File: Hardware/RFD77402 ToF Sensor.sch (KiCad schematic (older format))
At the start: 18 parts, among them J1 Qwiic_Connector, J2 Qwiic_Connector, J3 CONN_01X01, J4 I2C_Standard_PTH_Connector, U1 RFD77402, U2 SPARKX-LOGO4, U3 SPARKX-LOGO4, U4 CC_LICENSE

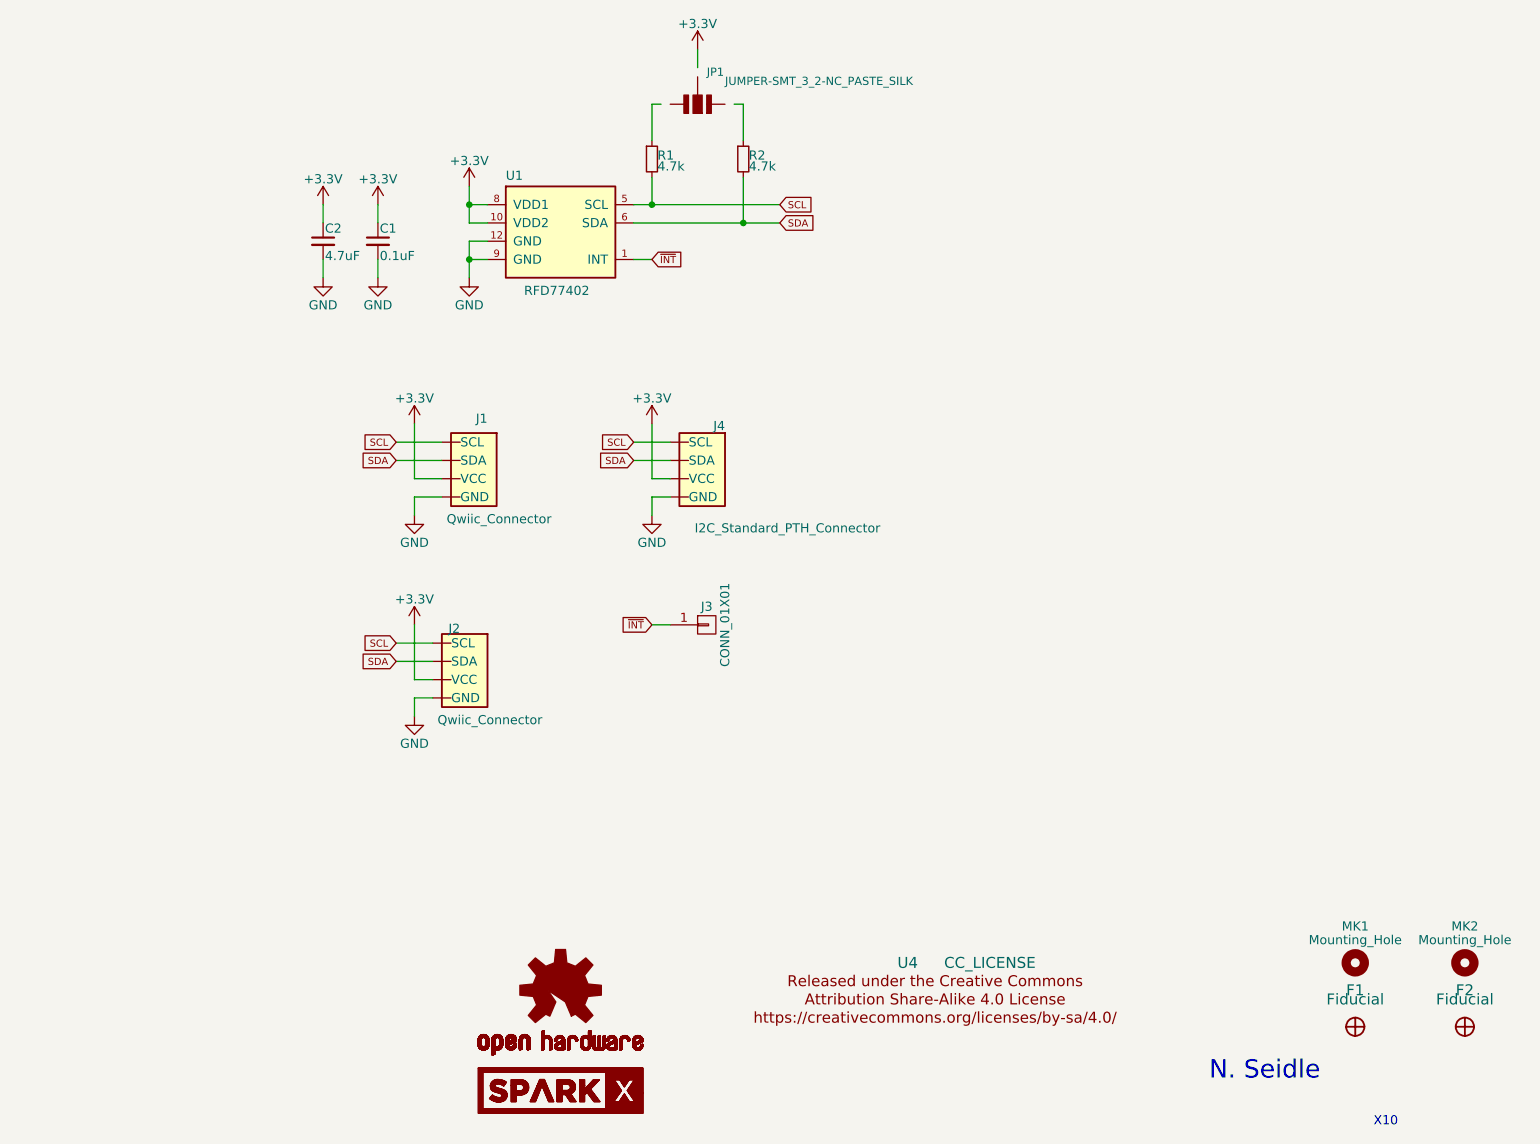
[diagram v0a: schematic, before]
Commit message: Decreasing paste on sensor
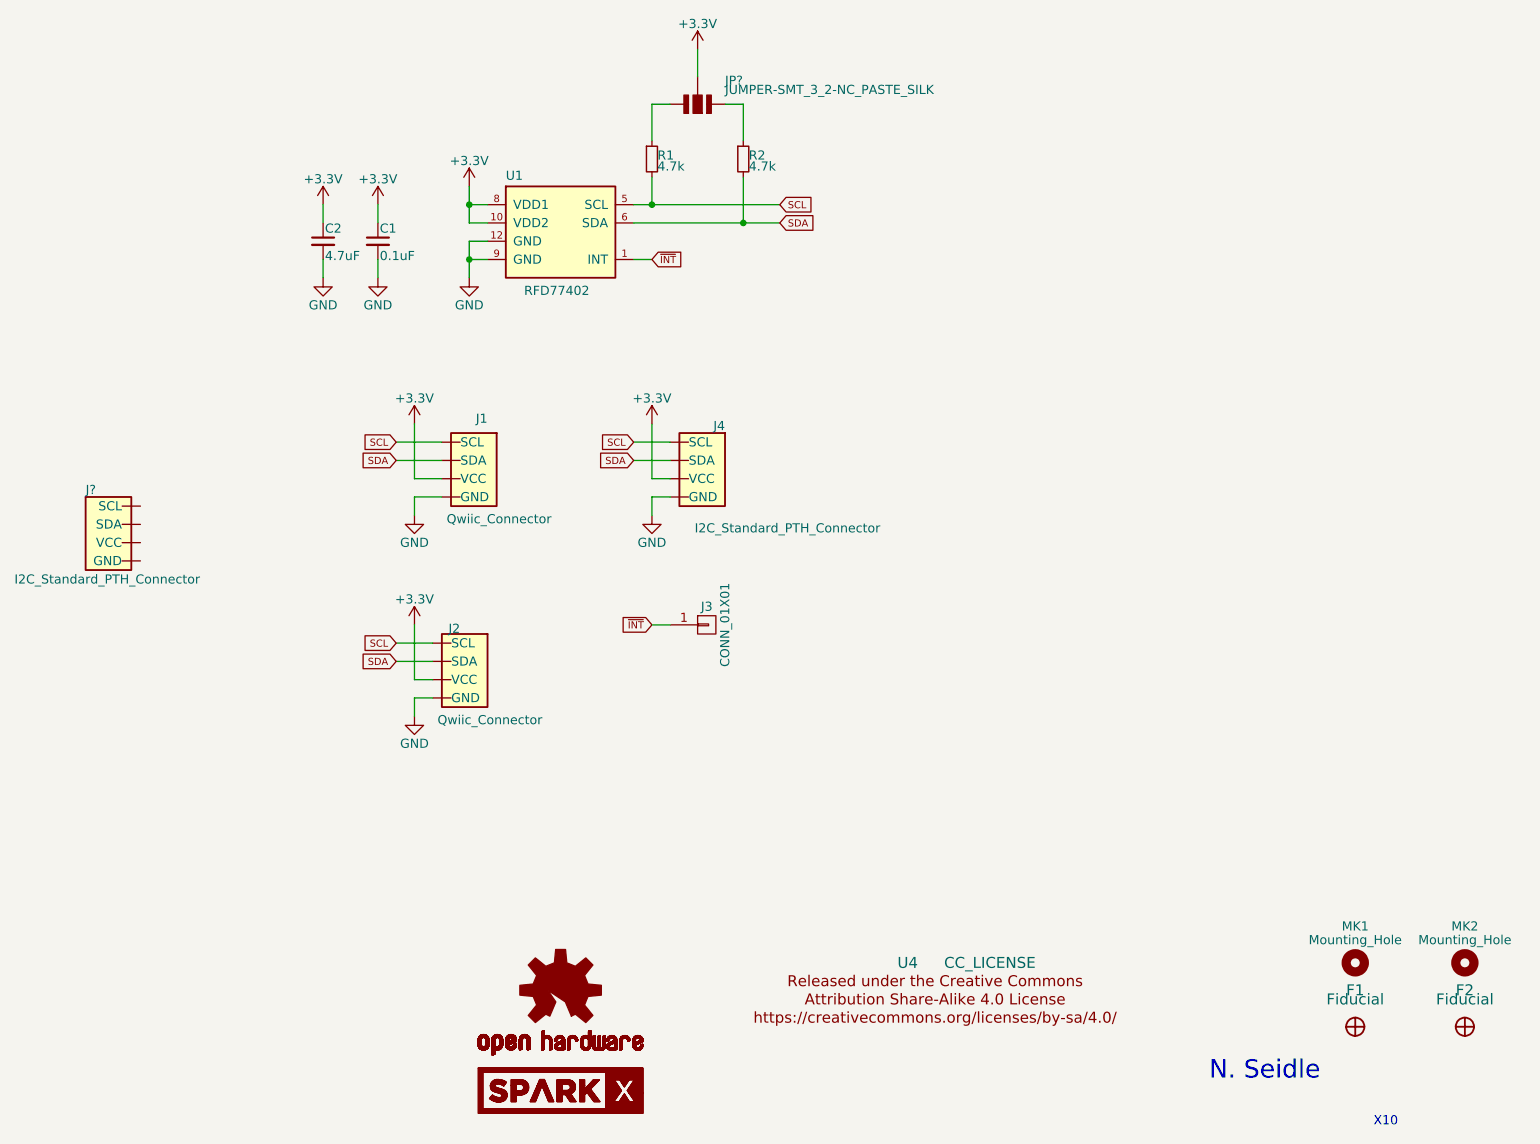
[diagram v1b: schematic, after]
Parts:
- removed JP1: JUMPER-SMT_3_2-NC_PASTE_SILK, SparkFun-Jumpers:SMT-JUMPER_3_2-NC_PASTE_SILK, symbol JUMPER-SMT_3_2-NC_PASTE_SILK
- added J?: I2C_Standard_PTH_Connector, symbol I2C_Standard_PTH_Connector
- added JP?: JUMPER-SMT_3_2-NC_PASTE_SILK, symbol JUMPER-SMT_3_2-NC_PASTE_SILK
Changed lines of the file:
@@
 EESchema Schematic File Version 2
+LIBS:RFD77402 ToF Sensor-rescue
+LIBS:74xgxx
+LIBS:74xx
+LIBS:ac-dc
+LIBS:actel
+LIBS:adc-dac
+LIBS:allegro
+LIBS:Altera
+LIBS:analog_devices
+LIBS:analog_switches
+LIBS:atmel
+LIBS:audio
+LIBS:battery_management
+LIBS:bbd
+LIBS:bosch
+LIBS:brooktre
+LIBS:cmos_ieee
+LIBS:cmos4000
+LIBS:conn
+LIBS:contrib
+LIBS:cypress
+LIBS:dc-dc
+LIBS:device
+LIBS:digital-audio
+LIBS:diode
+LIBS:display
+LIBS:dsp
+LIBS:elec-unifil
+LIBS:ESD_Protection
+LIBS:ftdi
+LIBS:gennum
+LIBS:graphic
+LIBS:hc11
+LIBS:intel
+LIBS:interface
+LIBS:ir
+LIBS:Lattice
+LIBS:leds
+LIBS:linear
+LIBS:logo
+LIBS:maxim
+LIBS:mechanical
+LIBS:memory
+LIBS:microchip
+LIBS:microchip_dspic33dsc
+LIBS:microchip_pic10mcu
+LIBS:microchip_pic12mcu
+LIBS:microchip_pic16mcu
+LIBS:microchip_pic18mcu
+LIBS:microchip_pic24mcu
+LIBS:microchip_pic32mcu
+LIBS:microcontrollers
+LIBS:modules
+LIBS:motor_drivers
+LIBS:motorola
+LIBS:motors
+LIBS:msp430
+LIBS:nordicsemi
+LIBS:nxp
+LIBS:nxp_armmcu
+LIBS:onsemi
+LIBS:opto
+LIBS:Oscillators
+LIBS:philips
 LIBS:power
-LIBS:conn
-LIBS:device
-LIBS:leds
-LIBS:mechanical
-LIBS:SparkFun-LED
-LIBS:SparkFun-Clocks
-LIBS:SparkFun-Aesthetics
-LIBS:SparkFun-Batteries
-LIBS:SparkFun-Boards
-LIBS:SparkFun-Capacitors
-LIBS:SparkFun-Coils
-LIBS:SparkFun-Connectors
-LIBS:SparkFun-DiscreteSemi
-LIBS:SparkFun-Electromechanical
-LIBS:SparkFun-Fuses
-LIBS:SparkFun-GPS
-LIBS:SparkFun-Hardware
-LIBS:SparkFun-IC-Amplifiers
-LIBS:SparkFun-Jumpers
+LIBS:Power_Management
+LIBS:powerint
+LIBS:pspice
+LIBS:references
+LIBS:regul
+LIBS:relays
+LIBS:rfcom
+LIBS:sensors
+LIBS:silabs
+LIBS:siliconi
+LIBS:stm8
+LIBS:stm32
+LIBS:supertex
+LIBS:switches
+LIBS:texas
+LIBS:transf
+LIBS:transistors
+LIBS:triac_thyristor
+LIBS:ttl_ieee
+LIBS:valves
+LIBS:video
+LIBS:wiznet
+LIBS:Worldsemi
+LIBS:Xicor
+LIBS:xilinx
+LIBS:zetex
+LIBS:Zilog
+LIBS:SparkX
 LIBS:RFD77402 ToF Sensor-cache
 EELAYER 25 0
@@
 	6450 2250 6450 2450
 Wire Wire Line
-	6450 2250 6400 2250
+	6350 2250 6450 2250
 Wire Wire Line
 	5950 2250 5950 2450
 Wire Wire Line
-	5950 2250 6000 2250
+	5950 2250 6050 2250
 Wire Wire Line
 	5850 2800 6650 2800
@@
 $EndComp
 Wire Wire Line
-	6200 1950 6200 2050
+	6200 1950 6200 2100
 $Comp
 L Qwiic_Connector J1
@@
 $EndComp
 $Comp
-L JUMPER-SMT_3_2-NC_PASTE_SILK JP1
-U 1 1 59082286
-P 6200 2250
-F 0 "JP1" V 6050 2300 45  0000 L BNN
-F 1 "JUMPER-SMT_3_2-NC_PASTE_SILK" V 6100 2400 45  0000 L BNN
-F 2 "SparkFun-Jumpers:SMT-JUMPER_3_2-NC_PASTE_SILK" H 6230 2400 20  0001 C CNN
-F 3 "" H 6200 2250 60  0001 C CNN
-	1    6200 2250
-	0    1    1    0
-$EndComp
-$Comp
 L I2C_Standard_PTH_Connector J4
 U 1 1 590843FA
@@
 Wire Wire Line
 	4150 2800 4150 2900
+$Comp
+L I2C_Standard_PTH_Connector J?
+U 1 1 593F72A4
+P 2950 4600
+F 0 "J?" H 2850 4810 50  0000 L BNN
+F 1 "I2C_Standard_PTH_Connector" H 2460 4320 50  0000 L BNN
+F 2 "" H 2930 4700 20  0001 C CNN
+F 3 "" H 2900 4550 60  0001 C CNN
+	1    2950 4600
+	1    0    0    -1
+$EndComp
+$Comp
+L JUMPER-SMT_3_2-NC_PASTE_SILK JP?
+U 1 1 593F0A1A
+P 6200 2250
+F 0 "JP?" V 6100 2400 50  0000 L BNN
+F 1 "JUMPER-SMT_3_2-NC_PASTE_SILK" V 6150 2400 50  0000 L BNN
+F 2 "" H 6200 2250 60  0001 C CNN
+F 3 "" H 6200 2250 60  0001 C CNN
+	1    6200 2250
+	0    1    1    0
+$EndComp
 $EndSCHEMATC
